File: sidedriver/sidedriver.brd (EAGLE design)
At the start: 70 x 72 mm, 31 parts, among them IC2 LT1086CM-3.3, Q1 8MHz

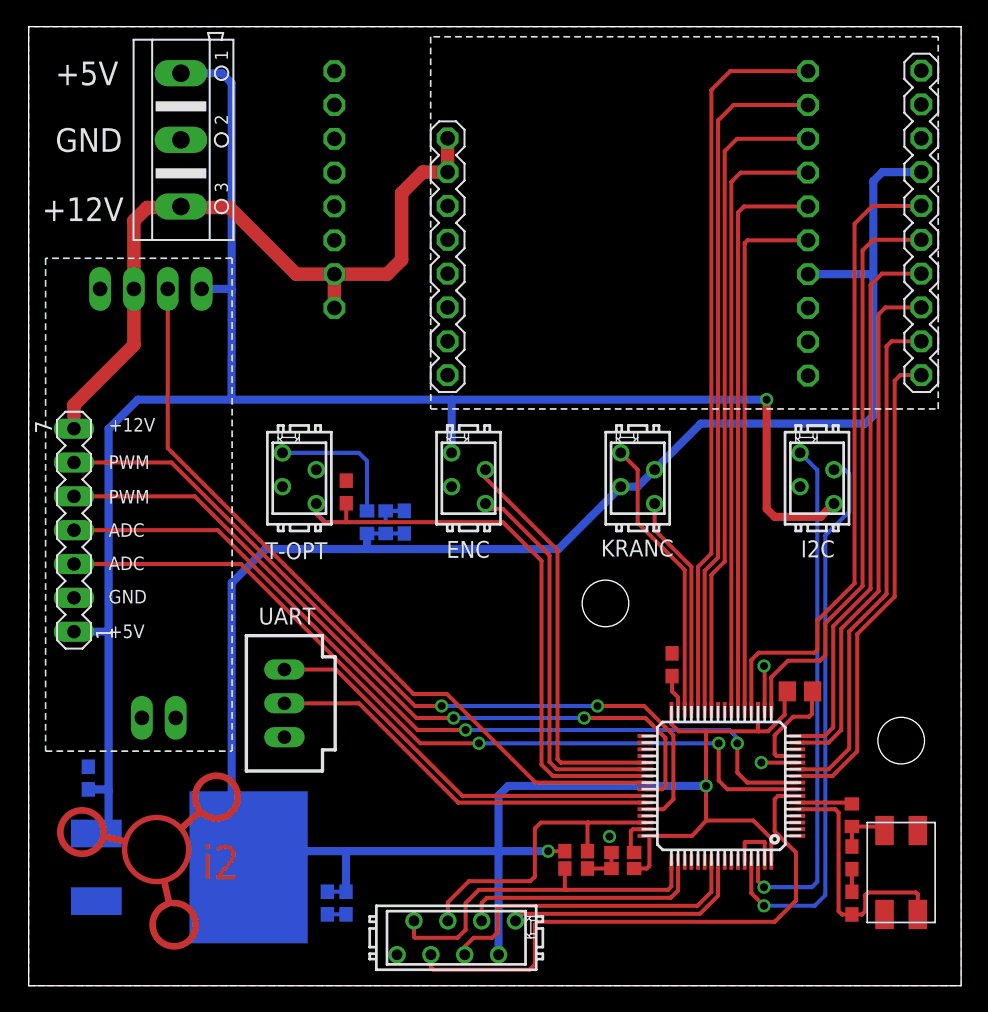
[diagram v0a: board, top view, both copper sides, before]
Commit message: sidedriver: PCB rev.2 created
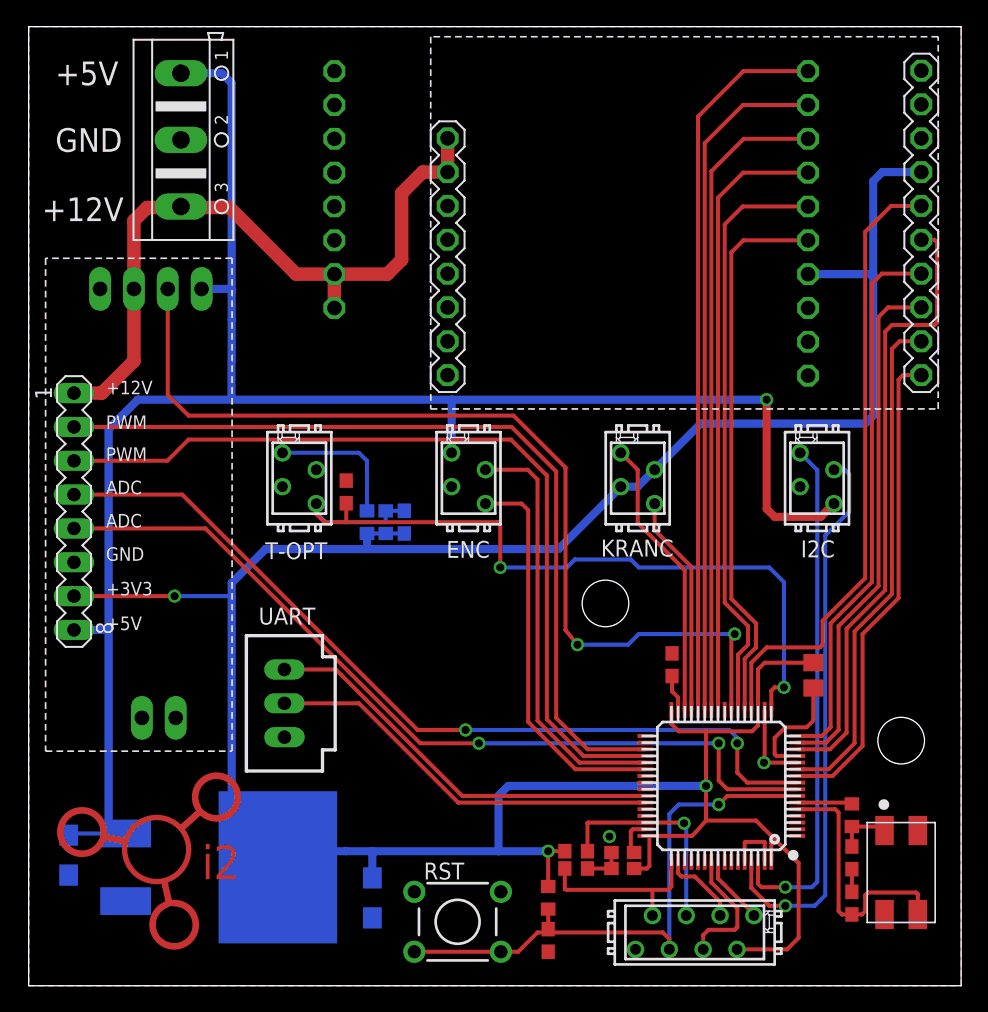
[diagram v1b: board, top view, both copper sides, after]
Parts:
- removed C10: i tu tez, rcl:C0603
- removed SV2: (no value), con-lstb:MA07-1
- added C11: 100n, rcl:C0603
- added R1: 100k, rcl:R0603
- added RST: (no value), wb_2:SWITCH
- added SV1: (no value), con-lstb:MA08-1
- C2: value i tu tez -> 10u; device rcl:C0603 -> rcl:SMC_A
- C3: value wartosc, tej -> 10u; device rcl:C0603 -> rcl:SMC_A
- moved C3 23.1 mm to (25.8, 6.60), turned to 270 degrees
- moved C2 19.8 mm to (3.00, 9.80)
- moved JTAG 17.9 mm to (50.0, 4.00)
- moved IC2 2.20 mm to (16.2, 8.89)
- moved L1 1.56 mm to (58.9, 23.3), turned to 270 degrees
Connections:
- new net N$2: U$1.58
- new net N$3: U$1.59
- new net N$6: U$1.44
- new net N$7: U$1.41
- net !RST: now also C11.2, R1.2, RST.2, RST.4
- net +12V: now also SV1.1; no longer SV2.7
- net +3V3: now also C3.+, R1.1, SV1.7; no longer C10.1, C2.1
- net +5V: now also C2.+, SV1.8; no longer C3.1, SV2.1
- net GND: now also C11.1, C2.-, C3.-, RST.1, RST.3, SV1.6; no longer C10.2, C2.2, C3.2, SV2.2
- net G_ADC1: now also SV1.5; no longer SV2.3
- net G_ADC2: now also SV1.4; no longer SV2.4
- net LED-PWM: now also U$1.23; no longer U$1.40
- net M1-ENB: now also U$1.14; no longer U$1.17
- net M2-CS: now also U$1.25; no longer U$1.23
- net SRV1: now also SV1.3, U$1.36; no longer SV2.5, U$1.41
- net SRV2: now also SV1.2, U$1.35; no longer SV2.6, U$1.44
- net TRANS: now also U$1.17; no longer U$1.39
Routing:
- net +3V3: track 198.3 -> 218.0 mm, vias 2 -> 3
- net JTDO: track 24.1 -> 9.59 mm
- net !JRST: track 18.6 -> 5.15 mm
- net JTCK: track 26.9 -> 13.5 mm
- net LED-PWM: track 58.2 -> 71.6 mm, vias 0 -> 2
- net JTDI: track 18.6 -> 5.92 mm
- net TRANS: track 52.5 -> 60.7 mm, vias 0 -> 2
- net SRV1: track 57.1 -> 64.1 mm, vias 2 -> 0
- net JTMS: track 23.0 -> 16.4 mm, vias 0 -> 1
- net M1-ENB: track 43.5 -> 47.0 mm
- net SRV2: track 60.7 -> 63.8 mm, vias 2 -> 0
- net +5V: track 133.8 -> 135.8 mm
- net M2-INB: track 39.9 -> 41.6 mm
- net M2-ENB: track 42.8 -> 44.3 mm
- net +12V: track 54.8 -> 53.3 mm
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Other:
- board text added: "+3V3"

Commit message: sidedriver: PCB rev.2 updates
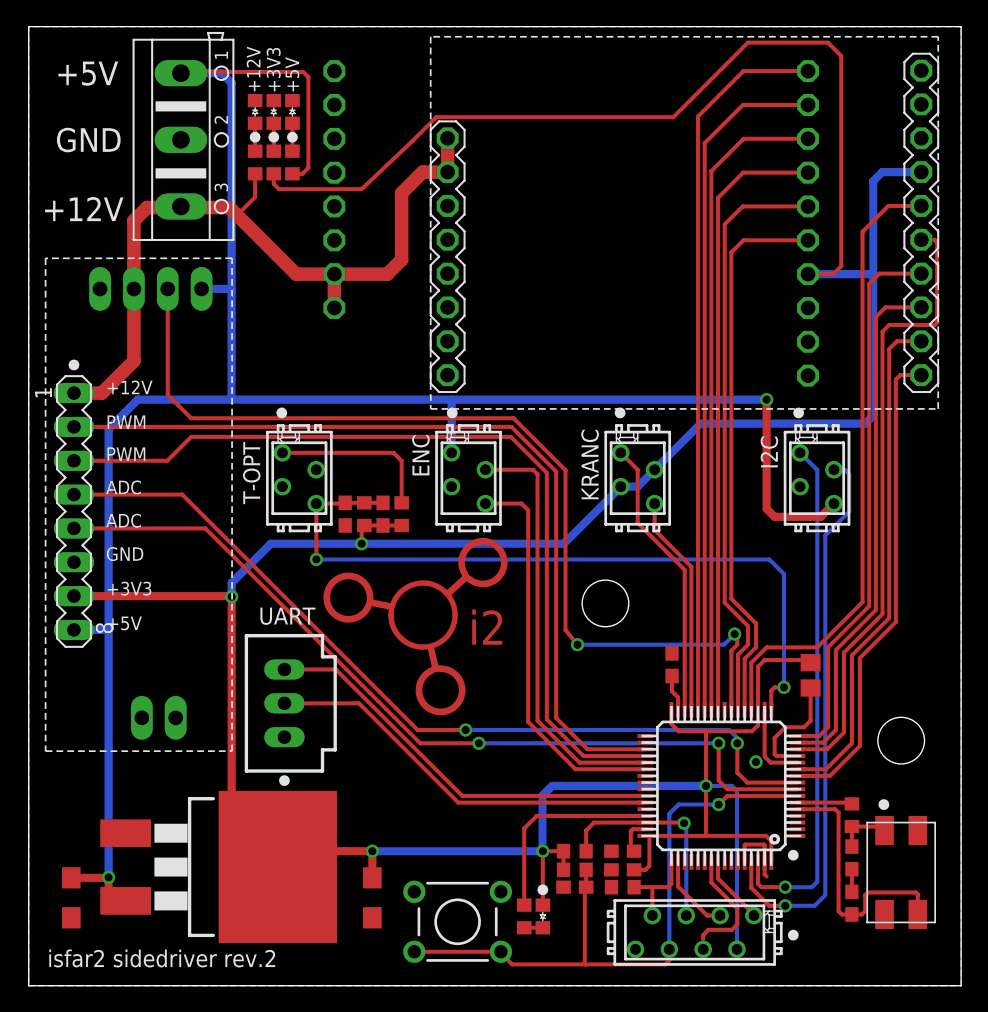
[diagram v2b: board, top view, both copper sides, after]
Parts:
- removed IC2: LT1086CM-3.3, v-reg:D2PACK
- added R10, R7, R8, R9: 500R, rcl:R0603
- added U$6, U$7, U$8, U$9: LED0603, wb:D0603
- added U2: LT1086CM-3.3, v-reg:D2PACK
- moved U$5 26.6 mm to (29.8, 28.2)
- moved C11 4.47 mm to (41.0, 7.40), turned to 0 degrees
- moved R6 3.77 mm to (44.6, 7.40), turned to 0 degrees
- moved C2 3.21 mm to (3.20, 6.60), flipped to the top
- moved R1 2.90 mm to (41.0, 8.70), turned to 0 degrees
- moved R2 2.67 mm to (28.0, 35.4), flipped to the top
- moved R3 1.71 mm to (25.2, 35.4), flipped to the top
- moved C4 1.71 mm to (26.6, 35.4), flipped to the top
- moved C1 1.67 mm to (23.8, 35.4), turned to 90 degrees
- moved L1 0.20 mm to (58.7, 23.3)
- moved C7 0.10 mm to (44.6, 8.70)
- moved R5 0.10 mm to (41.0, 10.1)
- moved C8 0.10 mm to (44.6, 10.1)
- flipped C3 to the top
- renumbered U$1 to U1
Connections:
- removed net N$2: U1.58
- removed net N$3: U1.59
- removed net N$6: U1.44
- removed net N$7: U1.41
- new net N$10: R9.2, U$8.1
- new net N$11: R10.2, U$9.2
- new net N$12: R10.1, U1.45
- new net N$8: R7.2, U$6.1
- new net N$9: R8.2, U$7.1
- net +12V: now also R7.1
- net +3V3: now also R9.1, U$9.1, U2.2; no longer IC2.2
- net +5V: now also R8.1, U2.3; no longer IC2.3
- net GND: now also U$6.2, U$7.2, U$8.2, U2.1; no longer IC2.1
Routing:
- net +3V3: track 218.0 -> 286.1 mm, vias 3 -> 5
- net +5V: track 135.8 -> 158.6 mm, vias 1 -> 2
- net N$12: track 0.00 -> 15.2 mm
- net JTCK: track 13.5 -> 6.69 mm
- net !RST: track 42.8 -> 48.2 mm
- net TRANS: track 60.7 -> 55.8 mm
- net +12V: track 53.3 -> 57.0 mm
- net GND: track 15.6 -> 13.0 mm, vias 2 -> 1
- net N$9: track 0.00 -> 2.10 mm
- net N$8: track 0.00 -> 2.10 mm
- net N$10: track 0.00 -> 2.10 mm
- net N$1: track 10.4 -> 12.4 mm
- net N$11: track 0.00 -> 1.40 mm
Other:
- board text added: "isfar2 sidedriver rev.2"
